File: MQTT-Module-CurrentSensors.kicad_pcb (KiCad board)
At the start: 4 copper layers, 44 x 55.9 mm, 65 parts, among them IC401 16 Bit ADC, J301 A2541WV-10P, J302 A2541WV-10P, J303 A2541WV-2x3P, J304 1715747, U202 ATmega328PB-A, U501 Precision ZD RR, U502 Precision ZD RR, U503 Precision ZD RR

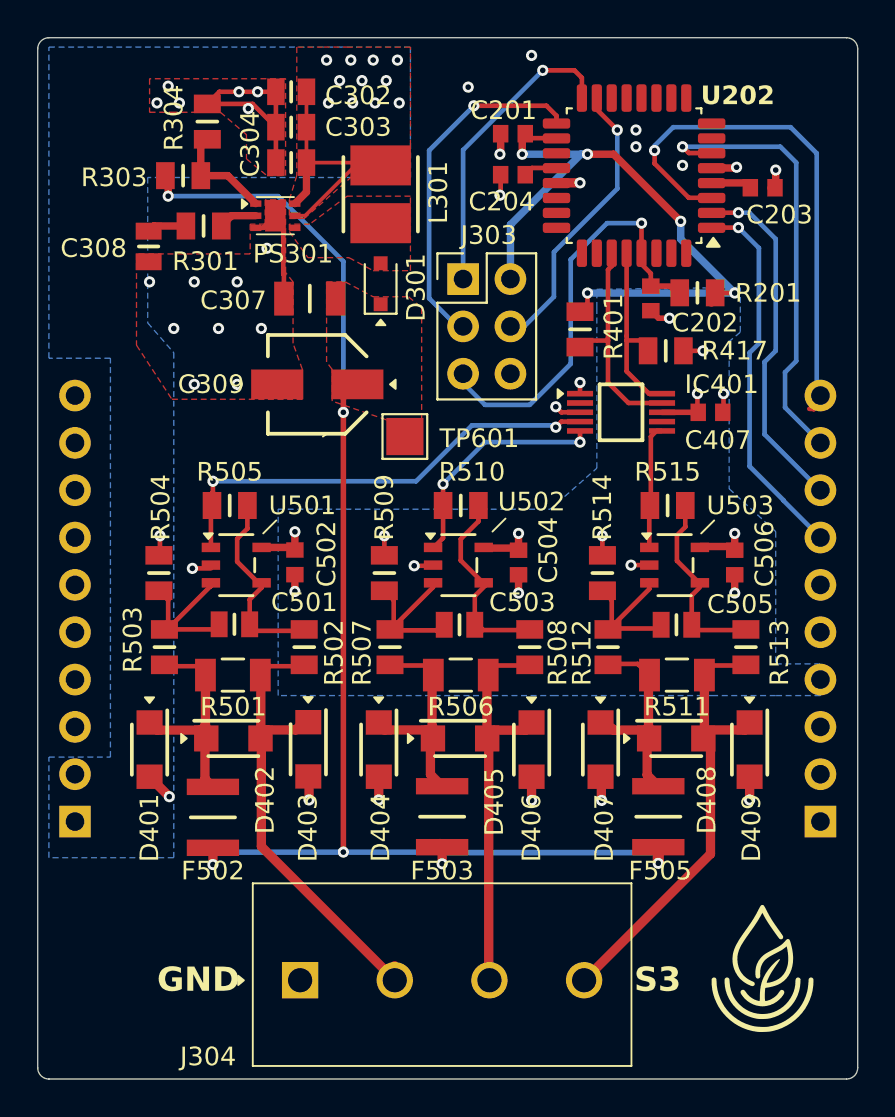
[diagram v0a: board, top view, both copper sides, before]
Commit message: Removed overflow on mask of ATMEGA. Reconnected traces, ran RRC checks, updated resolution of generated renders to 4k.
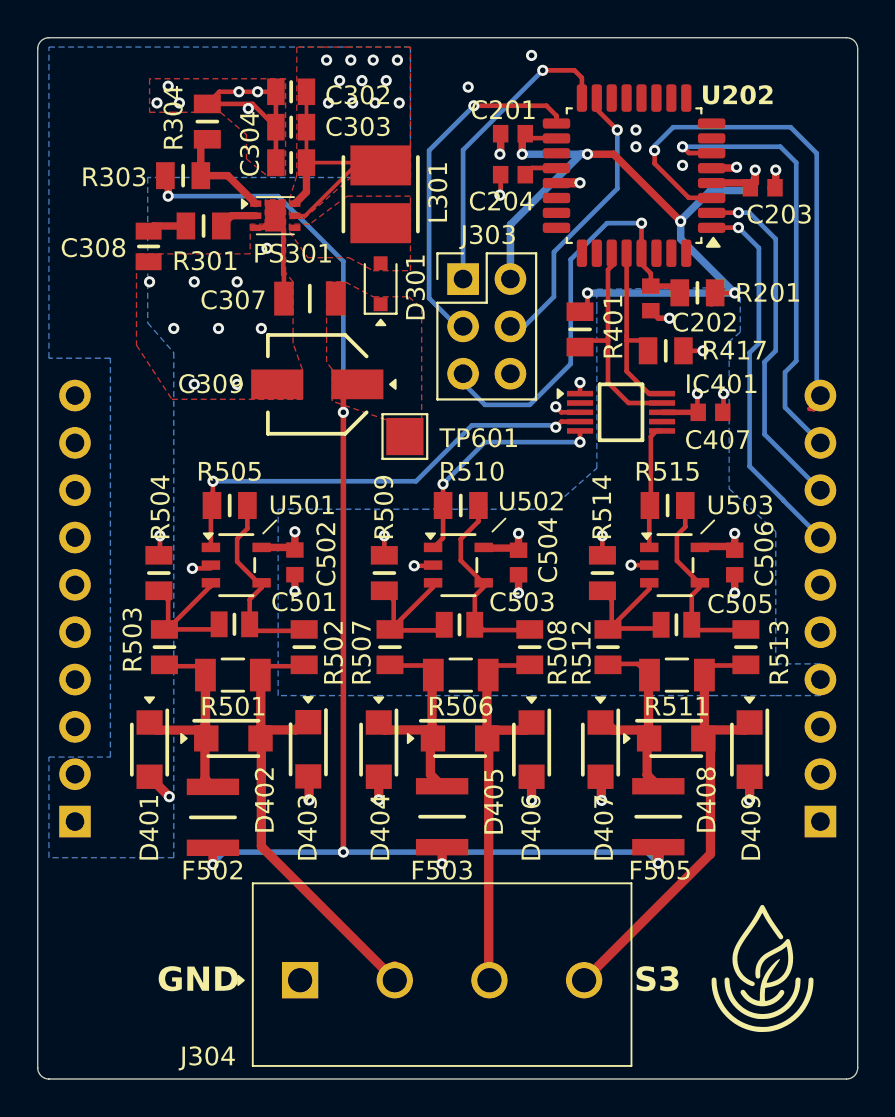
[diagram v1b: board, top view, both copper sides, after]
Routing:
- net +3V3: track 53.9 -> 60.4 mm, vias 10 -> 11
- net +25V: track 72.4 -> 73.5 mm

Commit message: Updated PCB, increased GND and improved connections on fills.
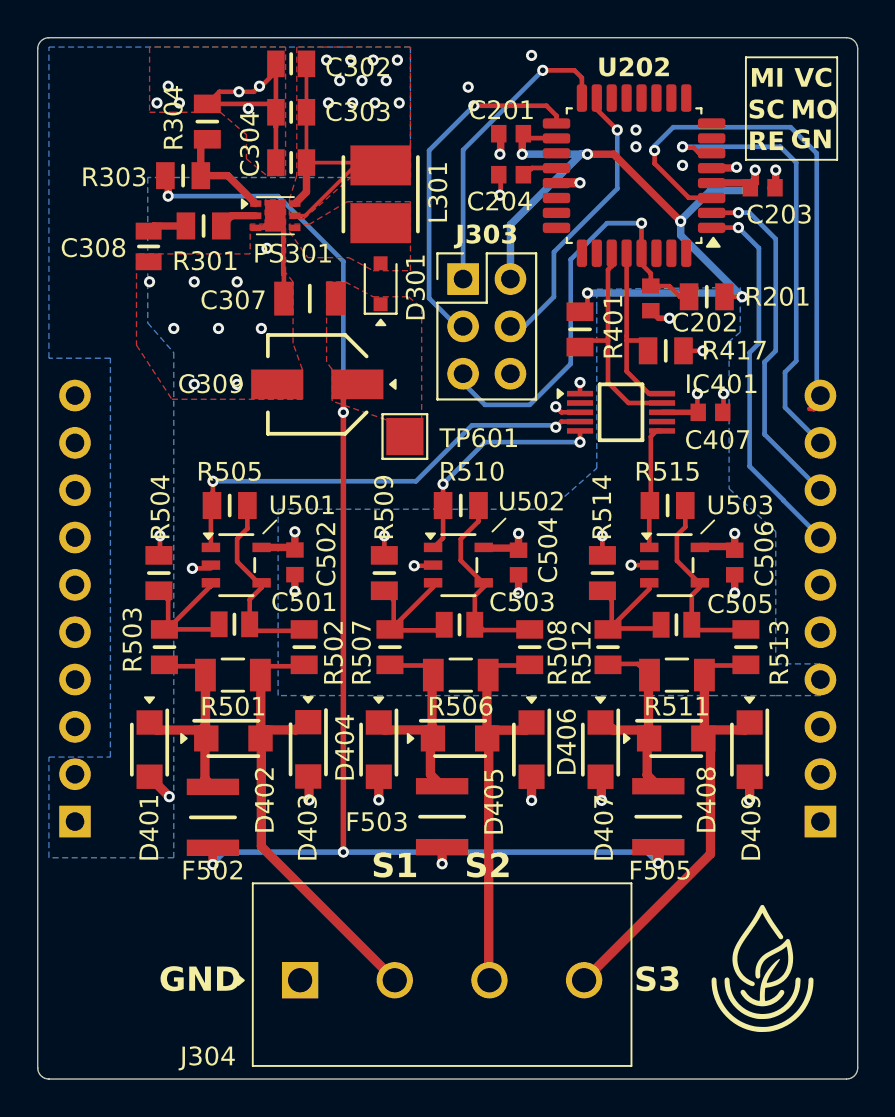
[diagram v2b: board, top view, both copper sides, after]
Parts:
- J303: footprint CJT Connectors:PinHeader_2x03_P2.54mm_Vertical -> CJT Connectors:PinHeader_2x03_P2.54mm_Vertical_Male
- moved C302 1.50 mm to (131.6, 69.4)
- moved C303 0.80 mm to (131.6, 72.0)
- moved R201 0.54 mm to (153.9, 81.9)
- moved C201 0.10 mm to (143.4, 73.2)
- moved C204 0.10 mm to (143.4, 75.3)
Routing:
- net GND: track 45.6 -> 48.6 mm
- net +12V: track 16.3 -> 17.8 mm
- net /SensorRecievers/Sensor1: track 26.0 -> 25.2 mm
- net /Controller/RESET: track 23.2 -> 23.7 mm
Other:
- board text added: "GN"
- board text added: "MI"
- board text added: "MO"
- board text added: "RE"
- board text added: "SC"
- board text added: "VC"
